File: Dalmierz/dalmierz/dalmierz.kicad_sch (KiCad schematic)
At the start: 51 parts, among them IC1 W25Q16JVUXIQ, J1 690-005-298-486, J2 B4B-ZR_LF__SN_TF LUNA, J3 B4B-ZR_LF__SN_LCD I2C, J7 B4B-ZR_LF__SN_URM13, SW1 1-1825910-4, SW2 1-1825910-4, SW3 1-1825910-4, SW4 1-1825910-4, SW5 1-1825910-4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

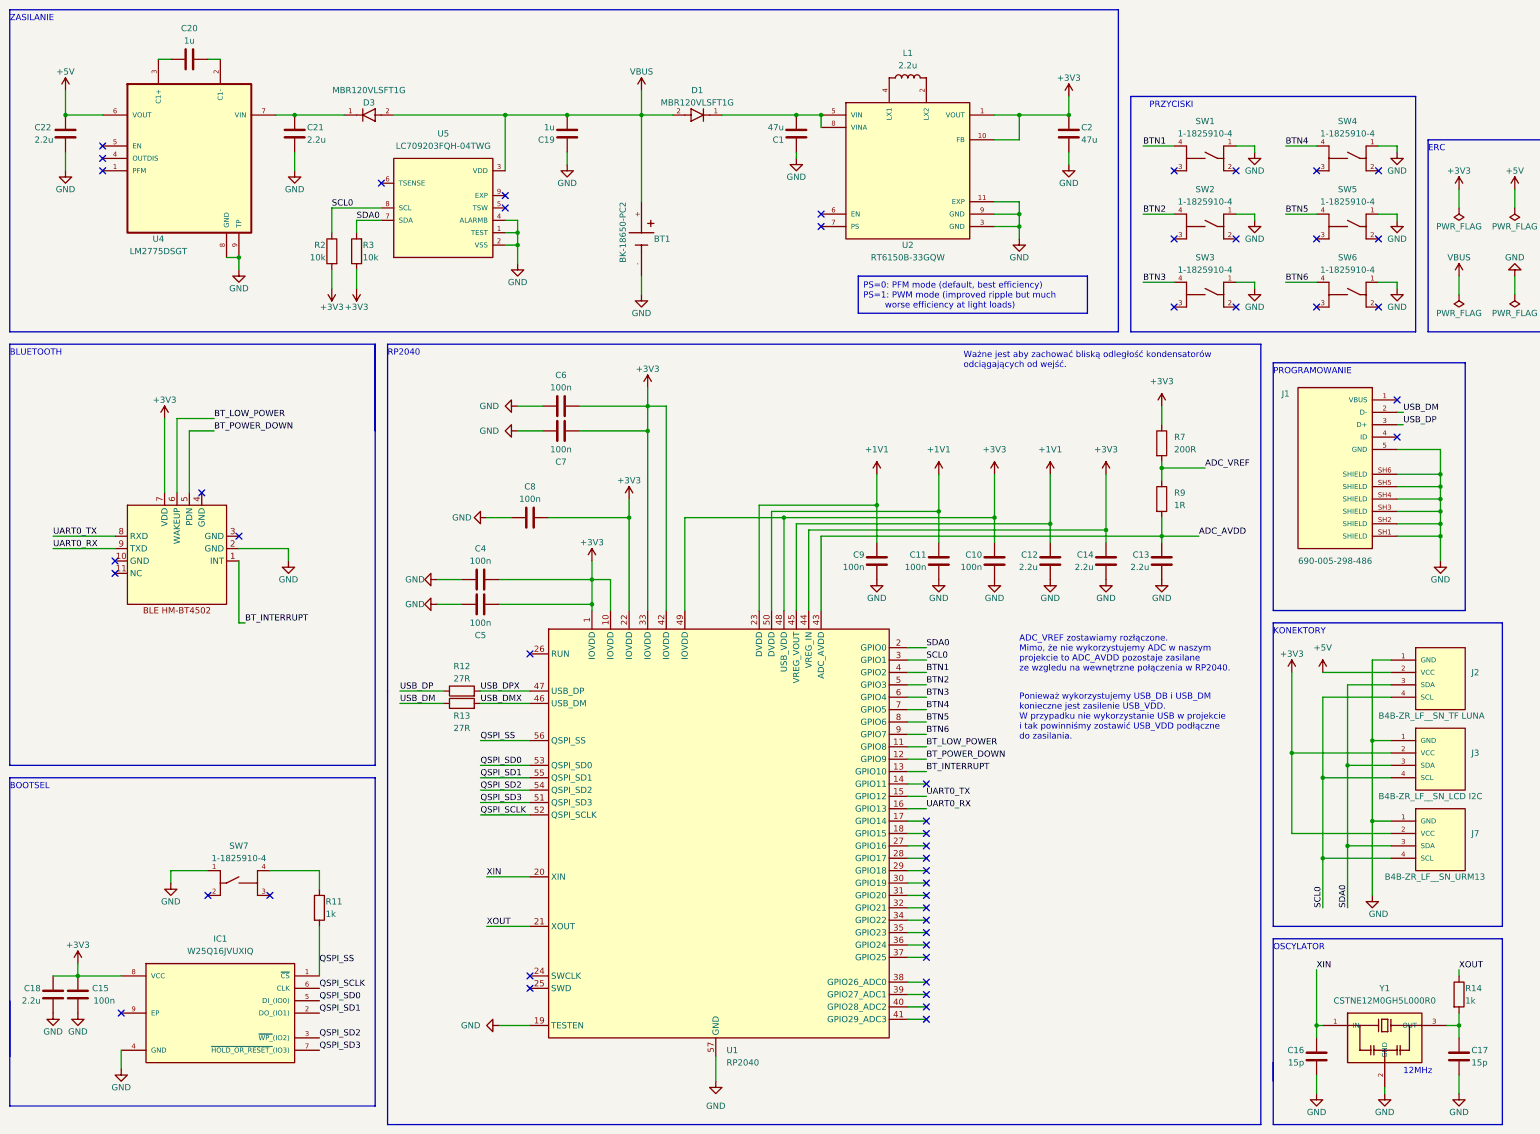
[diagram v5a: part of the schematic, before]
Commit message: MAIN: rozwiazanie problemow PCB
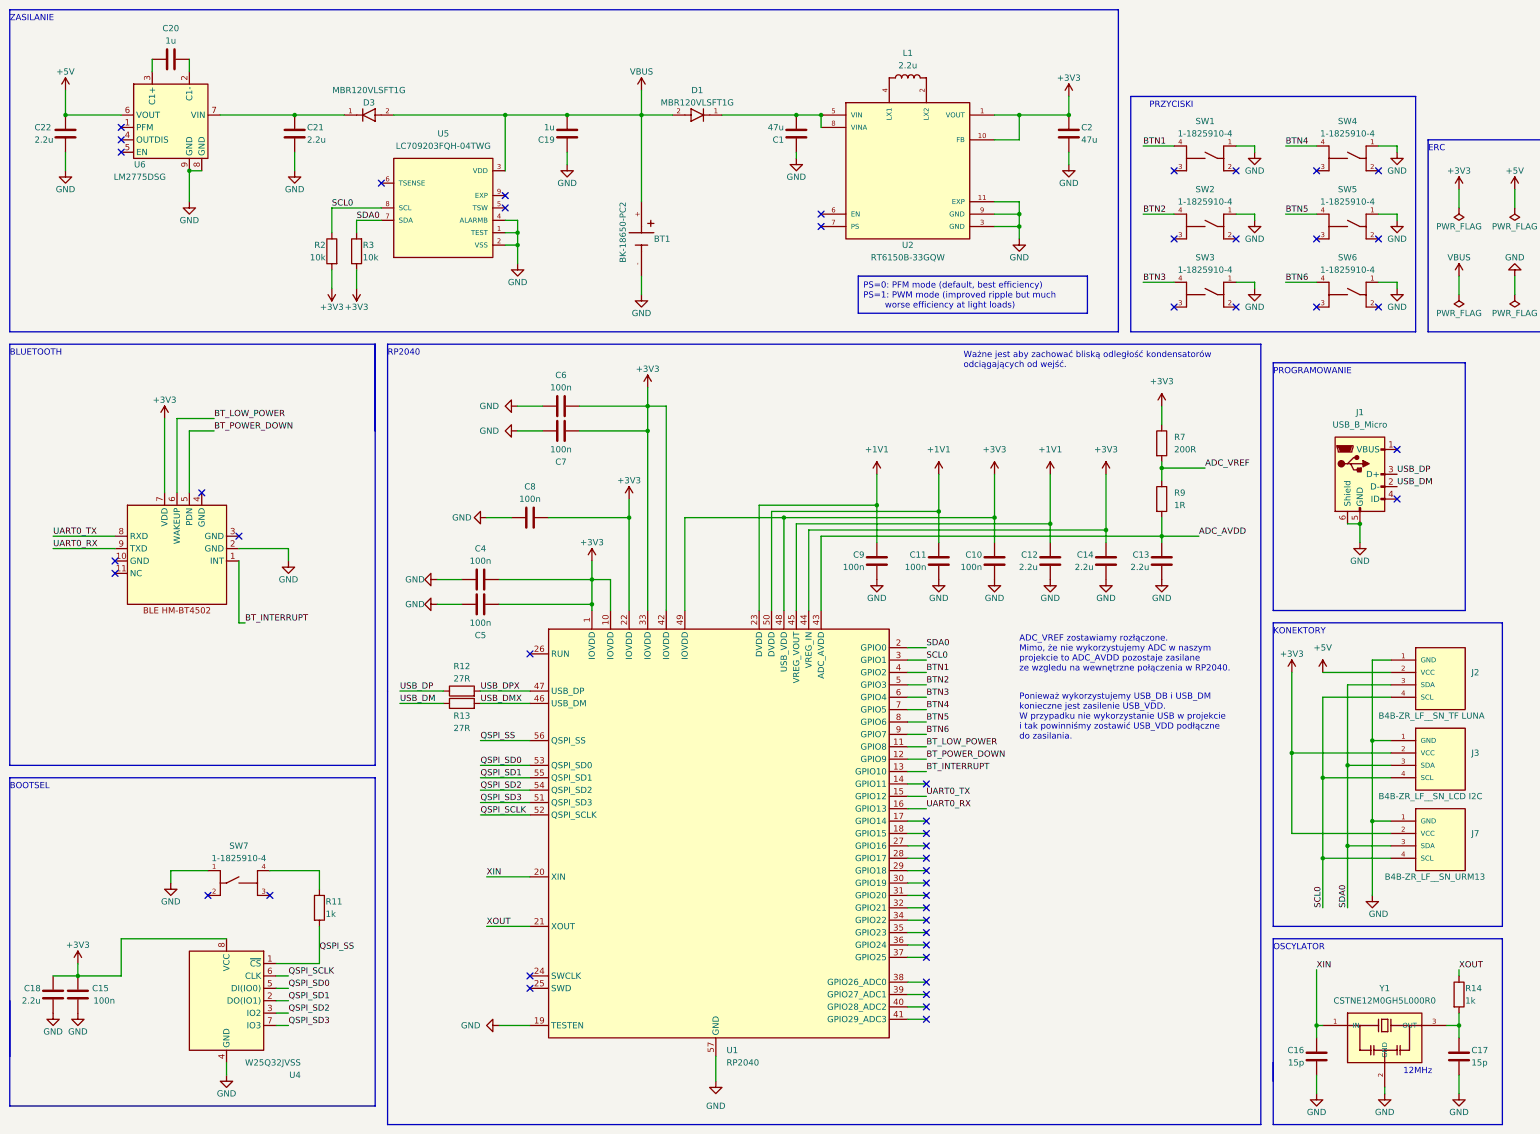
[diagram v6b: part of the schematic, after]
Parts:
- removed IC1: W25Q16JVUXIQ, W25Q16JVUXIQ:SON50P300X200X60-9N, symbol W25Q16JVUXIQ:W25Q16JVUXIQ
- removed J1: 690-005-298-486, 690-005-298-486:EDAC_690-005-298-486, symbol 690-005-298-486:690-005-298-486
- removed U4: LM2775DSGT, LM2775DSGT:SON50P200X200X80-9N, symbol LM2775DSGT:LM2775DSGT
- added J1: USB_B_Micro, Connector_USB:USB_Micro-B_Amphenol_10103594-0001LF_Horizontal, symbol Connector:USB_B_Micro
- added U4: W25Q32JVSS, Package_SO:SOIC-8_5.23x5.23mm_P1.27mm, symbol Memory_Flash:W25Q32JVSS
- added U6: LM2775DSG, Package_SON:WSON-8-1EP_2x2mm_P0.5mm_EP0.9x1.6mm, symbol LM2775DSG_custom:LM2775DSG
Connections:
- net +3V3: now also U4.8 (VCC)
- net +5V: now also U6.6 (VOUT)
- net GND: now also J1.5 (GND), J1.6 (Shield), U4.4 (GND), U6.8 (GND), U6.9 (GND)
- net QSPI_SCLK: now also U4.6 (CLK)
- net QSPI_SD0: now also U4.5 (DI(IO0))
- net QSPI_SD1: now also U4.2 (DO(IO1))
- net QSPI_SD2: now also U4.3 (IO2)
- net QSPI_SD3: now also U4.7 (IO3)
- net QSPI_SS: now also U4.1 (~{CS})
- net USB_DM: now also J1.2 (D-)
- net USB_DP: now also J1.3 (D+)
- net at C21.2, D3.1: now also U6.7 (VIN)
- net at C20.1: now also U6.2 (C1-)
- net at C20.2: now also U6.3 (C1+)
- no-connect marks 49 -> 48
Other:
- moved on the sheet: C20

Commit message: dalmierz koniec
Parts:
- added C3: 100n, Capacitor_SMD:C_0603_1608Metric, symbol Device:C
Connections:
- net +3V3: now also C3.2
- net GND: now also B1.10 (GND), B1.11 (NC), B1.3 (GND), B1.4 (GND), C3.1
- no-connect marks 48 -> 44
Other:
- title: Projekt PUEIE - Dalmierz -> Projekt PUEIE - Dalmierz laserowy
